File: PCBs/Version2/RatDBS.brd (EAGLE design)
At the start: 28.6 x 17.8 mm, 18 parts

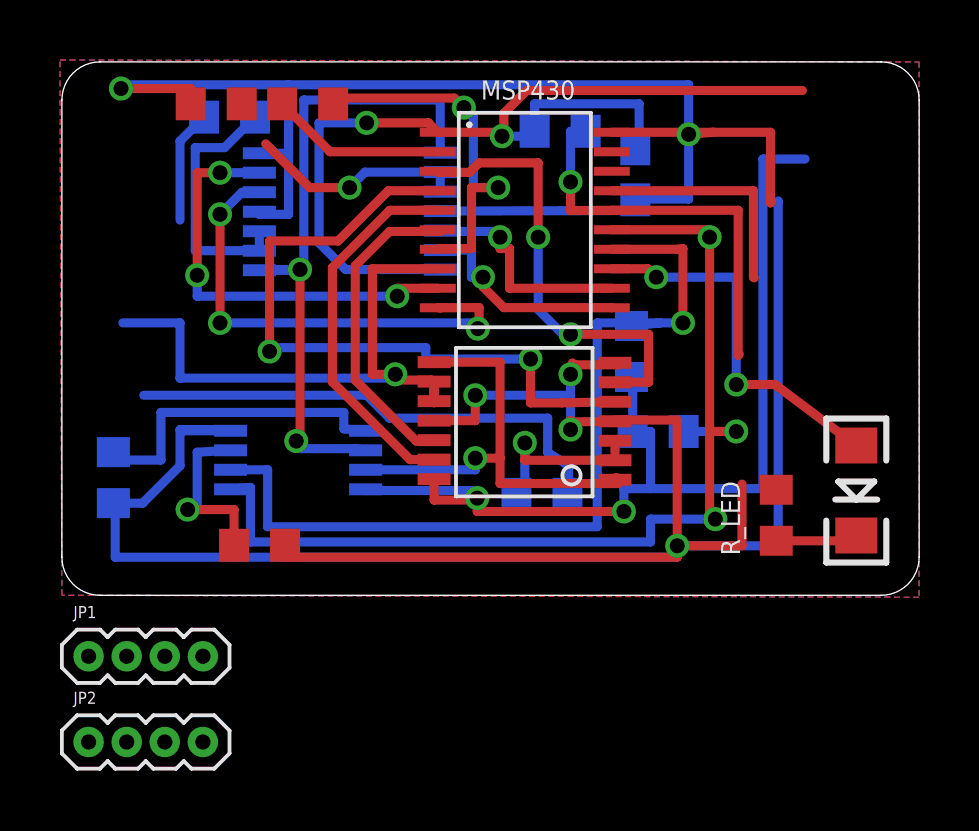
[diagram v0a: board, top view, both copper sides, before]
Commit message: Added single channel stimulator
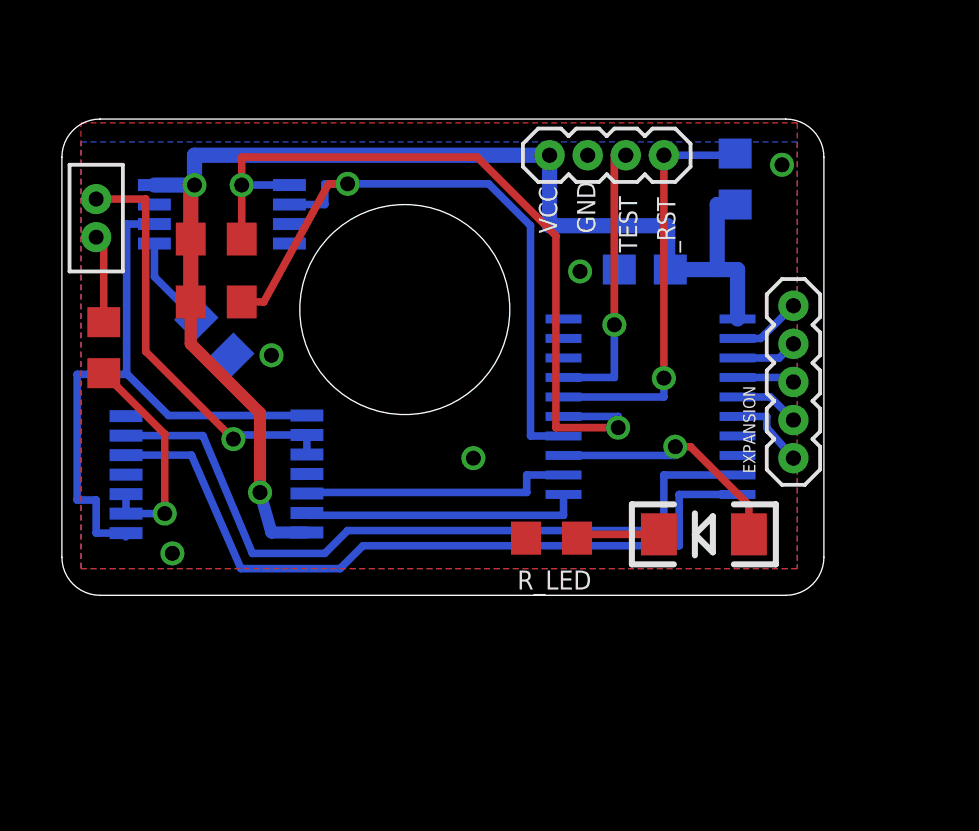
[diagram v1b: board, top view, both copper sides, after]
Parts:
- removed R_INPUT_FS1: 43k, BiphasicBoard:R0603
- removed R_LOAD_EX1: 10k, BiphasicBoard:R0603
- removed TS3A4751_1: (no value), BiphasicBoard:14_PIN
- removed V_DIV, V_DIV2: 1M, BiphasicBoard:R0603
- added EXPANSION: (no value), SparkFun:1X05-1.27MM
- JP2: value (none) -> FTSH-102; device SparkFun:1X04-1.27MM -> Samtec50Mil:FTSH-102-DH
- moved JP1 22.7 mm to (16.3, 14.7)
- moved JP2 17.5 mm to (1.14, 12.6), turned to 270 degrees
- moved R_PULLUP_SDA 16.1 mm to (5.14, 11.9), flipped to the top, turned to 180 degrees
- moved R_PULLUP_SCL 13.9 mm to (5.14, 9.78), flipped to the top, turned to 0 degrees
- moved TS3A4751_0 9.83 mm to (5.40, 3.24)
- moved R_LOAD_EX 8.75 mm to (1.40, 8.26), flipped to the top, turned to 270 degrees
- moved DS4432U+ 8.58 mm to (5.33, 12.7), turned to 0 degrees
- moved R_LED 7.53 mm to (16.3, 1.91), turned to 180 degrees
- moved MSP430 7.50 mm to (19.6, 6.29), flipped to the bottom
- moved R_PULLUP_RST 6.05 mm to (22.4, 13.9), turned to 270 degrees
- moved R_INPUT_FS0 5.78 mm to (5.08, 8.62), turned to 45 degrees
- moved LED6 5.29 mm to (21.4, 2.03), turned to 180 degrees
- moved C1_SUPPLY 3.19 mm to (19.4, 10.9), turned to 180 degrees
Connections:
- removed net DAC_OUT1: DS4432U+.7, TS3A4751_1.1, TS3A4751_1.8
- removed net IN1_1: MSP430.5, TS3A4751_1.13
- removed net IN2_1: MSP430.4, TS3A4751_1.5
- removed net IN3_1: MSP430.3, TS3A4751_1.6
- removed net IN4_1: MSP430.6, TS3A4751_1.12
- removed net LOAD1_1: R_LOAD_EX1.1, TS3A4751_1.2, TS3A4751_1.3
- removed net LOAD2_1: JP2.3, MSP430.8, TS3A4751_1.10, TS3A4751_1.9
- removed net VIA1: DS4432U+.3, R_INPUT_FS1.2
- new net N$10: EXPANSION.3, MSP430.4
- new net N$11: EXPANSION.4, MSP430.3
- new net N$12: EXPANSION.5, MSP430.2
- net GND: no longer R_INPUT_FS1.1, TS3A4751_1.11, TS3A4751_1.4, TS3A4751_1.7, V_DIV2.1
- net LOAD2_0: now also JP2.P$1; no longer JP2.1
- net N$3: now also EXPANSION.1, MSP430.6; no longer JP2.4, R_LOAD_EX1.2
- net N$4: now also JP2.P$2; no longer JP2.2
- net N$6: no longer V_DIV.2
- net N$7: now also EXPANSION.2, MSP430.5; no longer MSP430.2, V_DIV.1, V_DIV2.2
- net VDD: no longer TS3A4751_1.14
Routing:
- net GND: track 128.6 -> 0.00 mm, vias 6 -> 5
- net VDD: track 67.1 -> 42.6 mm, vias 4 -> 2
- net IN2_1: track 23.5 -> 0.00 mm, vias 2 -> 0
- net LOAD2_1: track 20.6 -> 0.00 mm, vias 1 -> 0
- net DAC_OUT1: track 15.3 -> 0.00 mm, vias 1 -> 0
- net IN3_1: track 15.1 -> 0.00 mm, vias 2 -> 0
- net N$3: track 16.7 -> 2.70 mm
- net IN1_1: track 12.6 -> 0.00 mm
- net N$6: track 12.3 -> 0.00 mm, vias 2 -> 0
- net IN4_1: track 10.7 -> 0.00 mm
- net IN3_0: track 14.5 -> 25.2 mm, vias 3 -> 0
- net IN2_0: track 16.3 -> 24.9 mm, vias 3 -> 0
- net N$2: track 34.5 -> 26.5 mm, vias 3 -> 2
- net N$8: track 10.7 -> 3.08 mm
- net LOAD2_0: track 7.29 -> 14.1 mm
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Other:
- board size 28.6 x 17.8 mm -> 25.4 x 15.9 mm
- board text added: "Biphasic v2.0 Kemere Lab 2015"
- board text added: "P1.2"
- board text added: "TEST"
- board text added: "_RST"
- board text removed: "Biphasic v1.3"
